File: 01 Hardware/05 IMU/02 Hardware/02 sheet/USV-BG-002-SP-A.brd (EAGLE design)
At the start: 70.8 x 50.1 mm, 5 parts, among them J2 690367291276, U1 RASPBERRY_PICOTH, X1 MKDSN1,5/3-5,08

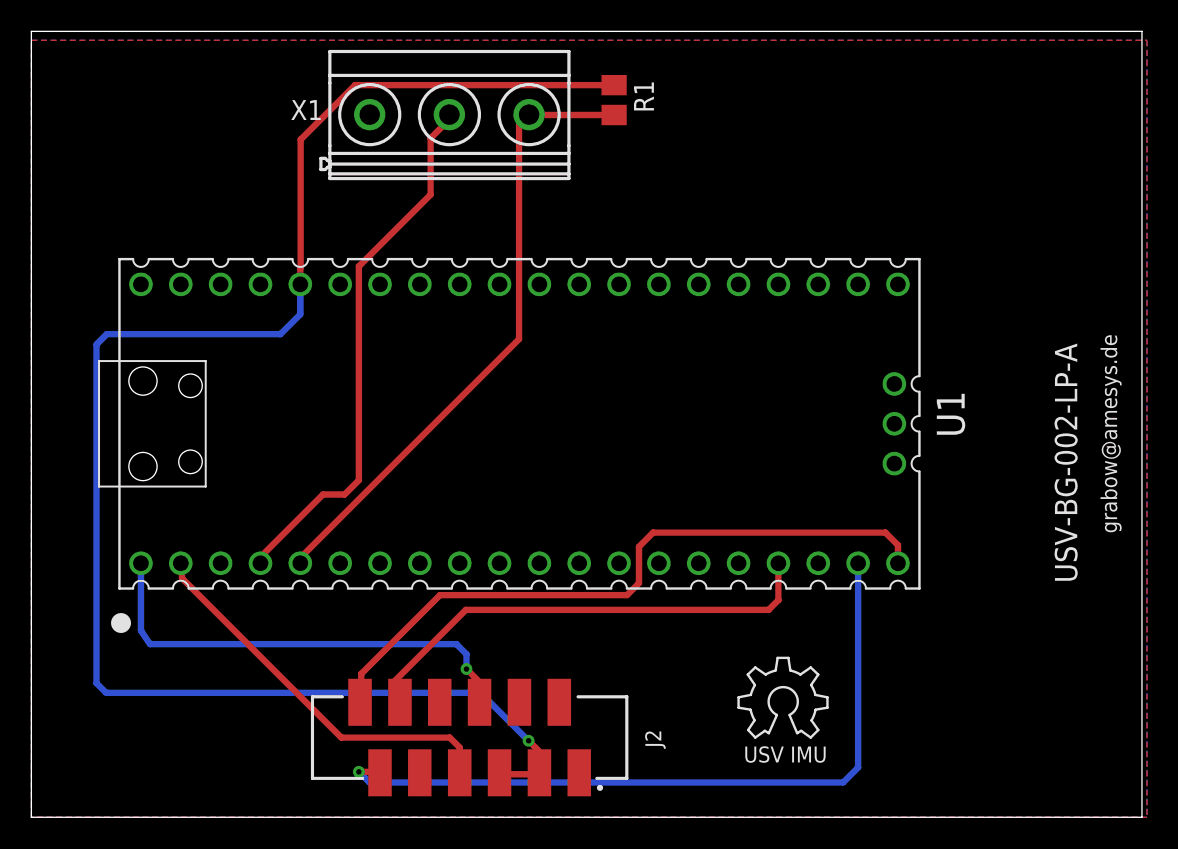
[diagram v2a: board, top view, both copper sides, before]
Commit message: new sheet und board design
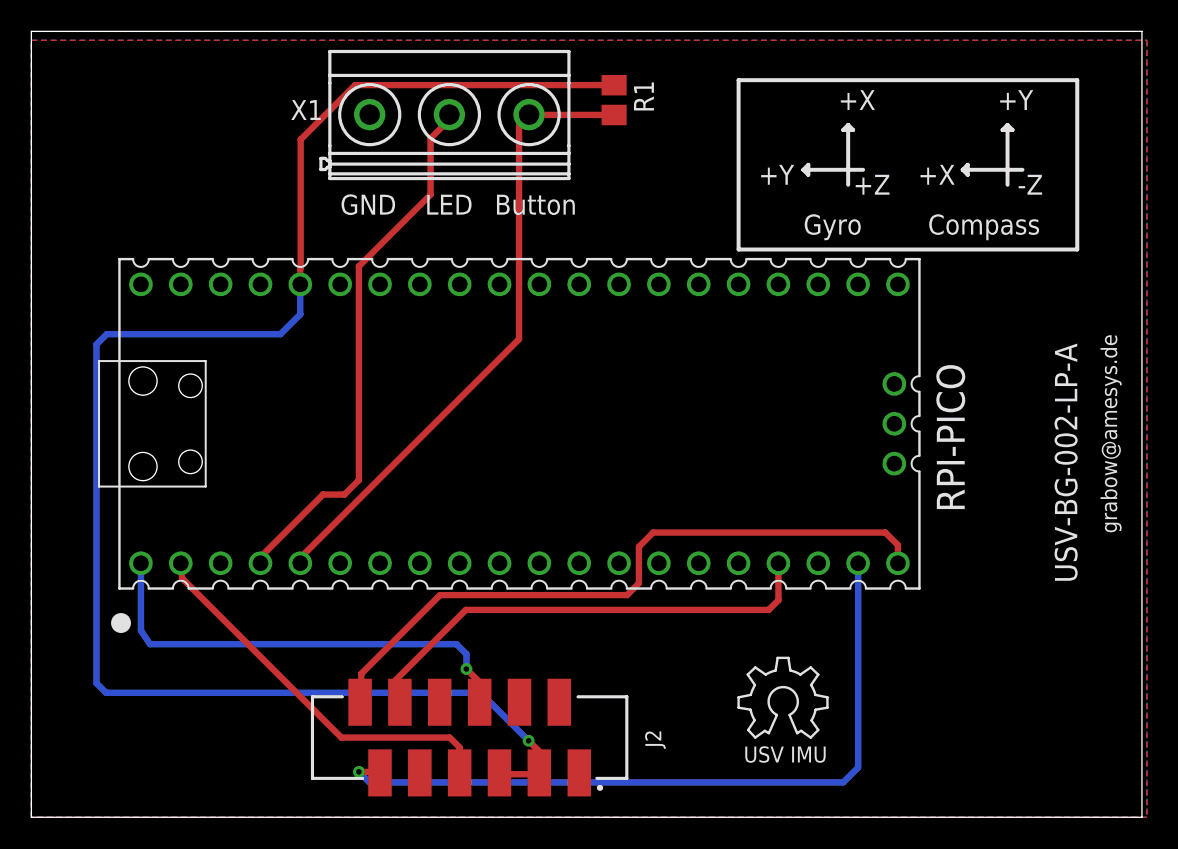
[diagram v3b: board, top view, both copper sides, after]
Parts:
- renumbered U1 to RPI-PICO
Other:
- board text added: "+X"
- board text added: "+Y"
- board text added: "+Z"
- board text added: "-Z"
- board text added: "Button"
- board text added: "Compass"
- board text added: "GND"
- board text added: "Gyro"
- board text added: "LED"
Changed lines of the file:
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@@
 <grid distance="0.0125" unitdist="inch" unit="inch" style="lines" multiple="1" display="no" altdistance="5" altunitdist="mil" altunit="mil"/>
 <layers>
-<layer number="1" name="Top" color="4" fill="1" visible="no" active="yes"/>
+<layer number="1" name="Top" color="4" fill="1" visible="yes" active="yes"/>
 <layer number="2" name="Route2" color="16" fill="1" visible="no" active="no"/>
 <layer number="3" name="Route3" color="17" fill="1" visible="no" active="no"/>
@@
 <layer number="49" name="Reference" color="7" fill="1" visible="no" active="yes"/>
 <layer number="50" name="dxf" color="7" fill="1" visible="no" active="no"/>
-<layer number="51" name="tDocu" color="7" fill="1" visible="no" active="yes"/>
+<layer number="51" name="tDocu" color="7" fill="1" visible="yes" active="yes"/>
 <layer number="52" name="bDocu" color="7" fill="1" visible="no" active="yes"/>
 <layer number="53" name="tGND_GNDA" color="7" fill="9" visible="no" active="no"/>
@@
 <text x="66.675" y="14.9225" size="1.4224" layer="25" font="vector" rot="R90">USV-BG-002-LP-A</text>
 <text x="45.4025" y="3.4925" size="1.016" layer="25" font="vector">USV IMU</text>
+<wire x1="49.2125" y1="41.275" x2="53.0225" y2="41.275" width="0.254" layer="25"/>
+<wire x1="52.07" y1="40.3225" x2="52.07" y2="44.1325" width="0.254" layer="25"/>
+<text x="46.355" y="40.3225" size="1.27" layer="25">+Y</text>
+<text x="51.435" y="45.085" size="1.27" layer="25">+X</text>
+<text x="49.2125" y="37.1475" size="1.27" layer="25">Gyro</text>
+<wire x1="59.3725" y1="41.275" x2="63.1825" y2="41.275" width="0.254" layer="25"/>
+<wire x1="62.23" y1="40.3225" x2="62.23" y2="44.1325" width="0.254" layer="25"/>
+<text x="56.515" y="40.3225" size="1.27" layer="25">+X</text>
+<text x="61.595" y="45.085" size="1.27" layer="25">+Y</text>
+<text x="57.15" y="37.1475" size="1.27" layer="25">Compass</text>
+<text x="52.3875" y="39.6875" size="1.27" layer="25">+Z</text>
+<text x="62.865" y="39.6875" size="1.27" layer="25">-Z</text>
+<wire x1="62.23" y1="44.1325" x2="61.9125" y2="43.815" width="0.254" layer="25"/>
+<wire x1="61.9125" y1="43.815" x2="62.5475" y2="43.815" width="0.254" layer="25"/>
+<wire x1="62.5475" y1="43.815" x2="62.23" y2="44.1325" width="0.254" layer="25"/>
+<wire x1="59.3725" y1="41.275" x2="59.69" y2="41.5925" width="0.254" layer="25"/>
+<wire x1="59.69" y1="41.5925" x2="59.69" y2="40.9575" width="0.254" layer="25"/>
+<wire x1="59.69" y1="40.9575" x2="59.3725" y2="41.275" width="0.254" layer="25"/>
+<wire x1="52.07" y1="44.1325" x2="52.3875" y2="43.815" width="0.254" layer="25"/>
+<wire x1="52.3875" y1="43.815" x2="51.7525" y2="43.815" width="0.254" layer="25"/>
+<wire x1="51.7525" y1="43.815" x2="52.07" y2="44.1325" width="0.254" layer="25"/>
+<wire x1="49.2125" y1="41.275" x2="49.53" y2="41.5925" width="0.254" layer="25"/>
+<wire x1="49.53" y1="41.5925" x2="49.53" y2="40.9575" width="0.254" layer="25"/>
+<wire x1="49.53" y1="40.9575" x2="49.2125" y2="41.275" width="0.254" layer="25"/>
+<wire x1="45.085" y1="46.99" x2="66.675" y2="46.99" width="0.254" layer="25"/>
+<wire x1="66.675" y1="46.99" x2="66.675" y2="36.195" width="0.254" layer="25"/>
+<wire x1="66.675" y1="36.195" x2="45.085" y2="36.195" width="0.254" layer="25"/>
+<wire x1="45.085" y1="36.195" x2="45.085" y2="46.99" width="0.254" layer="25"/>
+<text x="25.0825" y="38.4175" size="1.27" layer="25">LED</text>
+<text x="29.5275" y="38.4175" size="1.27" layer="25">Button</text>
+<text x="19.685" y="38.4175" size="1.27" layer="25">GND</text>
 </plain>
 <attributes>
@@
 </element>
 <element name="U$1" library="ohw-logo" package="OSHW_6X200_NOTEXT" value="" x="45.085" y="5.08" smashed="yes"/>
-<element name="U1" library="RpiPico" package="PICO-PKG-TH" value="RASPBERRY_PICOTH" x="31.115" y="25.0825" smashed="yes" rot="R90">
-<attribute name="NAME" x="59.4995" y="24.1935" size="1.778" layer="25" rot="R90"/>
+<element name="RPI-PICO" library="RpiPico" package="PICO-PKG-TH" value="RASPBERRY_PICOTH" x="31.115" y="25.0825" smashed="yes" rot="R90">
+<attribute name="NAME" x="59.4995" y="19.431" size="1.778" layer="25" rot="R90"/>
 <attribute name="VALUE" x="46.6725" y="26.0985" size="1.778" layer="27" rot="R180"/>
 </element>
@@
 <vertex x="0" y="0"/>
 </polygon>
-<contactref element="U1" pad="28"/>
-<contactref element="U1" pad="33"/>
-<contactref element="U1" pad="8"/>
-<contactref element="U1" pad="23"/>
-<contactref element="U1" pad="38"/>
-<contactref element="U1" pad="18"/>
-<contactref element="U1" pad="3"/>
-<contactref element="U1" pad="13"/>
-<contactref element="U1" pad="37"/>
+<contactref element="RPI-PICO" pad="28"/>
+<contactref element="RPI-PICO" pad="33"/>
+<contactref element="RPI-PICO" pad="8"/>
+<contactref element="RPI-PICO" pad="23"/>
+<contactref element="RPI-PICO" pad="38"/>
+<contactref element="RPI-PICO" pad="18"/>
+<contactref element="RPI-PICO" pad="3"/>
+<contactref element="RPI-PICO" pad="13"/>
+<contactref element="RPI-PICO" pad="37"/>
 <contactref element="X1" pad="1"/>
 </signal>
@@
 <wire x1="23.4696" y1="7.4676" x2="23.1648" y2="7.7724" width="0.1524" layer="1"/>
 <wire x1="23.4696" y1="7.4676" x2="23.495" y2="7.33" width="0.1524" layer="1"/>
-<contactref element="U1" pad="17"/>
+<contactref element="RPI-PICO" pad="17"/>
 <wire x1="23.1648" y1="8.6868" x2="23.1648" y2="7.7724" width="0.1524" layer="1"/>
 <wire x1="27.6987" y1="13.2207" x2="23.1648" y2="8.6868" width="0.4064" layer="1"/>
@@
 <wire x1="22.2504" y1="2.8956" x2="22.7076" y2="3.3528" width="0.1524" layer="1"/>
 <wire x1="22.2504" y1="2.8956" x2="22.225" y2="2.83" width="0.1524" layer="1"/>
-<contactref element="U1" pad="19"/>
+<contactref element="RPI-PICO" pad="19"/>
 <wire x1="22.7076" y1="3.3528" x2="22.225" y2="2.83" width="0.1524" layer="1"/>
 <wire x1="52.705" y1="16.1925" x2="52.705" y2="3.175" width="0.4064" layer="16"/>
@@
 <wire x1="21.0312" y1="7.4676" x2="21.0312" y2="8.2296" width="0.1524" layer="1"/>
 <wire x1="21.0312" y1="7.4676" x2="20.955" y2="7.33" width="0.1524" layer="1"/>
-<contactref element="U1" pad="20"/>
+<contactref element="RPI-PICO" pad="20"/>
 <wire x1="21.0312" y1="9.144" x2="21.0312" y2="8.2296" width="0.4064" layer="1"/>
 <wire x1="26.0477" y1="14.1605" x2="21.0312" y2="9.144" width="0.4064" layer="1"/>
@@
 <wire x1="32.4612" y1="3.6576" x2="32.4612" y2="2.8956" width="0.1524" layer="1"/>
 <wire x1="32.4612" y1="2.8956" x2="32.385" y2="2.83" width="0.1524" layer="1"/>
-<contactref element="U1" pad="36"/>
+<contactref element="RPI-PICO" pad="36"/>
 <wire x1="32.4612" y1="4.1148" x2="32.4612" y2="3.6576" width="0.1524" layer="1"/>
 <wire x1="31.6992" y1="4.8768" x2="32.4612" y2="4.1148" width="0.4064" layer="1"/>
@@
 </signal>
 <signal name="VSYS">
-<contactref element="U1" pad="39"/>
+<contactref element="RPI-PICO" pad="39"/>
 </signal>
 <signal name="VBUS">
-<contactref element="U1" pad="40"/>
+<contactref element="RPI-PICO" pad="40"/>
 </signal>
 <signal name="SWGND">
-<contactref element="U1" pad="42"/>
+<contactref element="RPI-PICO" pad="42"/>
 </signal>
 <signal name="UART0_TX">
-<contactref element="U1" pad="1"/>
+<contactref element="RPI-PICO" pad="1"/>
 <contactref element="J2" pad="6"/>
 <wire x1="28.4988" y1="7.4676" x2="28.575" y2="7.33" width="0.1524" layer="1"/>
@@
 </signal>
 <signal name="UART0_RX">
-<contactref element="U1" pad="2"/>
+<contactref element="RPI-PICO" pad="2"/>
 <contactref element="J2" pad="7"/>
 <wire x1="27.2796" y1="2.8956" x2="27.305" y2="2.83" width="0.1524" layer="1"/>
@@
 </signal>
 <signal name="LED/IO2">
-<contactref element="U1" pad="4"/>
+<contactref element="RPI-PICO" pad="4"/>
 <contactref element="X1" pad="2"/>
 <wire x1="14.6304" y1="16.6116" x2="14.6304" y2="16.3068" width="0.1524" layer="1"/>
@@
 </signal>
 <signal name="TA/IO3">
-<contactref element="U1" pad="5"/>
+<contactref element="RPI-PICO" pad="5"/>
 <contactref element="R1" pad="2"/>
 <contactref element="X1" pad="3"/>
